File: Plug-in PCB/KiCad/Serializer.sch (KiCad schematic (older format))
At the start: 32 parts, among them J1 Conn_Coaxial, U1 DS90UB933-Q1

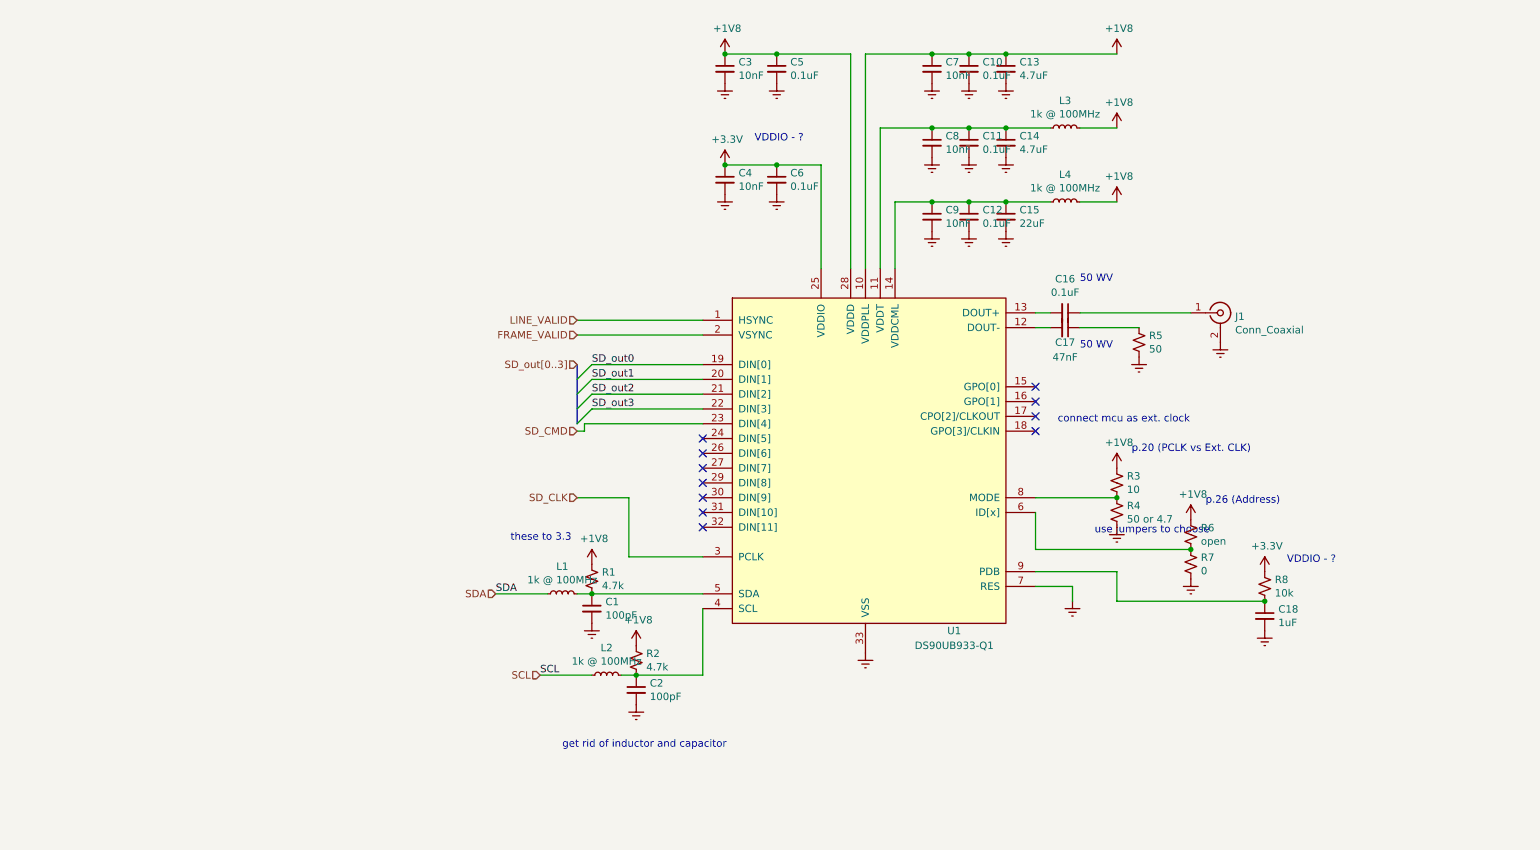
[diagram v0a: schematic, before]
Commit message: Wired Expansion Board Update
1. Begin hardcoding bit-bang communication between wirefree MCU and wired expansion MCU.
++ Can I use the PIO module on the pins to send data in sync while grabbing image from the sensor with parallel capture mode?

2. Wired expansion board schematics and layout modifications
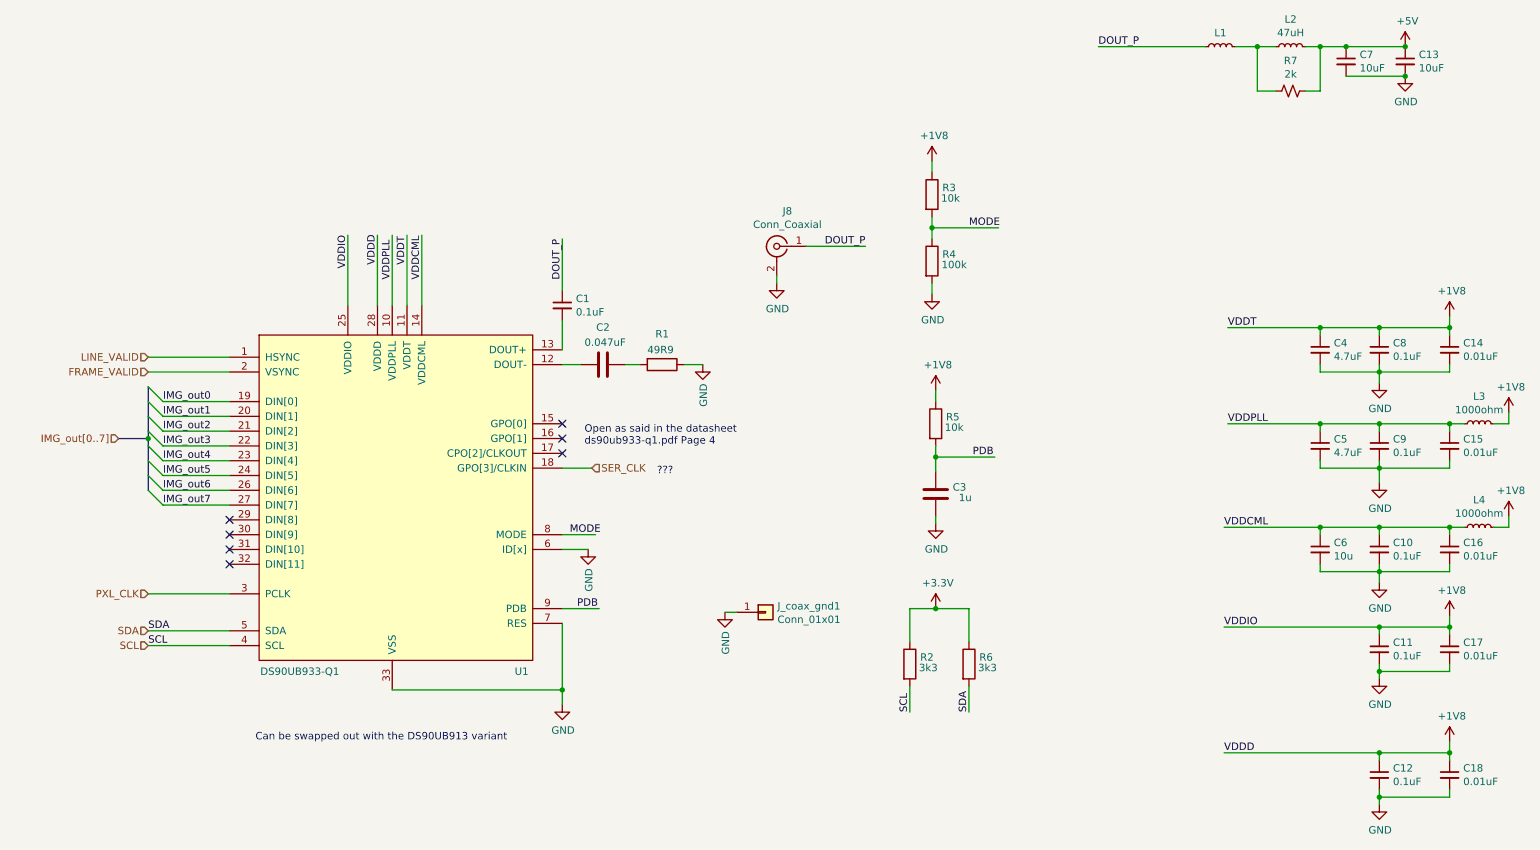
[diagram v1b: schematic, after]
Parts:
- removed C1, C2: GQM1875C2E101JB12D, .Capacitor:C_0603_1608Metric_L, symbol .Capacitor:GQM1875C2E101JB12D
- removed C10, C11, C12, C16, C5, C6: GCJ188R71E104KA12D, .Capacitor:C_0603_1608Metric_L, symbol .Capacitor:GCJ188R71E104KA12D
- removed C13, C14: GRM188R61E475KE11D, .Capacitor:C_0603_1608Metric_L, symbol .Capacitor:GRM188R61E475KE11D
- removed C15: GRM21BR61C226ME44L, .Capacitor:C_0805_2012Metric_L, symbol .Capacitor:GRM21BR61C226ME44L
- removed C17: GRM155R71E473KA88D, .Capacitor:C_0402_1005Metric_L, symbol .Capacitor:GRM155R71E473KA88D
- removed C18: GCM21BR71E105KA56L, .Capacitor:C_0805_2012Metric_L, symbol .Capacitor:GCM21BR71E105KA56L
- removed C3, C4, C7, C8, C9: GRM033R71A103KA01D, .Capacitor:C_0201_0603Metric_L, symbol .Capacitor:GRM033R71A103KA01D
- removed J1: Conn_Coaxial, .Connector:SMA-J-P-H-RA-TH1, symbol Connector:Conn_Coaxial
- removed L2: 1k @ 100MHz, .Inductor:L_0603_1608Metric_L, symbol .Device:L_Small
- removed R1, R2: 4.7k, .Resistor:R_0402_1005Metric_ERJ_L, symbol Device:R_Small_US
- removed R3: 10, .Resistor:R_0402_1005Metric_ERJ_L, symbol .Device:R_Small_US
- removed R4: 50 or 4.7, .Resistor:R_0402_1005Metric_ERJ_L, symbol .Device:R_Small_US
- removed R5: 50, .Resistor:R_0402_1005Metric_ERJ_L, symbol Device:R_Small_US
- removed R6: open, .Resistor:R_0402_1005Metric_ERJ_L, symbol .Device:R_Small_US
- removed R8: 10k, .Resistor:R_0402_1005Metric_ERJ_L, symbol .Device:R_Small_US
- added C1: GRM033R61A104ME15D, .Capacitor:C_0201_0603Metric_L, symbol .Capacitor:GRM033R61A104ME15D
- added C10, C11, C12, C8, C9: GRM033R61A104ME15D, .Capacitor:C_0201_0603Metric_L, symbol .Device:C_Small
- added C13, C7: GRM155R60J106ME15D, .Capacitor:C_0402_1005Metric_L, symbol .Capacitor:GRM155R60J106ME15D
- added C14, C15, C16, C17, C18: GRM033R71A103KA01D, .Capacitor:C_0201_0603Metric_L, symbol .Device:C_Small
- added C2: GRM033R61C473KE84D, .Capacitor:C_0201_0603Metric_L, symbol .Device:C
- added C3: GRM033R61A105ME15D, .Capacitor:C_0201_0603Metric_L, symbol .Device:C
- added C4, C5: GRM155R60J475ME47D, .Capacitor:C_0402_1005Metric_L, symbol .Device:C_Small
- added C6: GRJ155R60J106ME11D, .Capacitor:C_0402_1005Metric_L, symbol .Device:C_Small
- added J8: Conn_Coaxial, .Connector:U_FL-R-SMT_10_, symbol Connector:Conn_Coaxial
- added J_coax_gnd1: Conn_01x01, .Connector:Conn_1x1_100x100_Pad, symbol .Connector:Conn_01x01
- added L2: ADL3225V-470MT-TL000, .Inductor:L_1210_3225Metric_L, symbol .Inductor:ADL3225V-470MT-TL000
- added R1: ERJ-1GEF49R9C, .Resistor:R_0201_0603Metric_ERJ_L, symbol Device:R
- added R2, R6: ERJ-1GEF3321C, .Resistor:R_0201_0603Metric_ERJ_L, symbol Device:R
- added R3, R5: ERJ-1GEF1002C, .Resistor:R_0201_0603Metric_ERJ_L, symbol Device:R
- added R4: ERJ-1GEF1003C, .Resistor:R_0201_0603Metric_ERJ_L, symbol Device:R
- L1, L3, L4: value 1k @ 100MHz -> BLM15HD102SN1D; footprint .Inductor:L_0603_1608Metric_L -> Inductor_SMD:L_0402_1005Metric; Note (none) -> 1000ohm
- R7: value 0 -> MMBT3904LP-7B; footprint .Resistor:R_0402_1005Metric_ERJ_L -> .Resistor:R_0201_0603Metric_ERJ_L; Note (none) -> 2k; Size (none) -> 0201
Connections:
- net labels added: +5V, DOUT_P, GND, IMG_out0, IMG_out1, IMG_out2, IMG_out3, IMG_out4, IMG_out5, IMG_out6, IMG_out7, IMG_out[0..7], MODE, PDB, PXL_CLK, SER_CLK, VDDCML, VDDD, VDDIO, VDDPLL, VDDT
- net labels removed: Earth, SD_CLK, SD_CMD, SD_out0, SD_out1, SD_out2, SD_out3, SD_out[0..3]
- wire segments 54 -> 121
- no-connect marks 11 -> 7
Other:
- note added: "???"
- note added: "Can be swapped out with the DS90UB913 variant"
- note added: "Open as said in the datasheet\nds90ub933-q1.pdf Page 4"
- note removed: "50 WV"
- note removed: "VDDIO - ?"
- note removed: "connect mcu as ext. clock"
- note removed: "get rid of inductor and capacitor"
- note removed: "p.20 (PCLK vs Ext. CLK)"
- note removed: "p.26 (Address)"
- note removed: "these to 3.3"
- note removed: "use jumpers to choose"

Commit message: Wired Expansion Board Updates
1. KiCad: Schematics and layouts completed/Gerber files generated
2. Atmel: Communication protocol from WireFree to WiredExpansion written
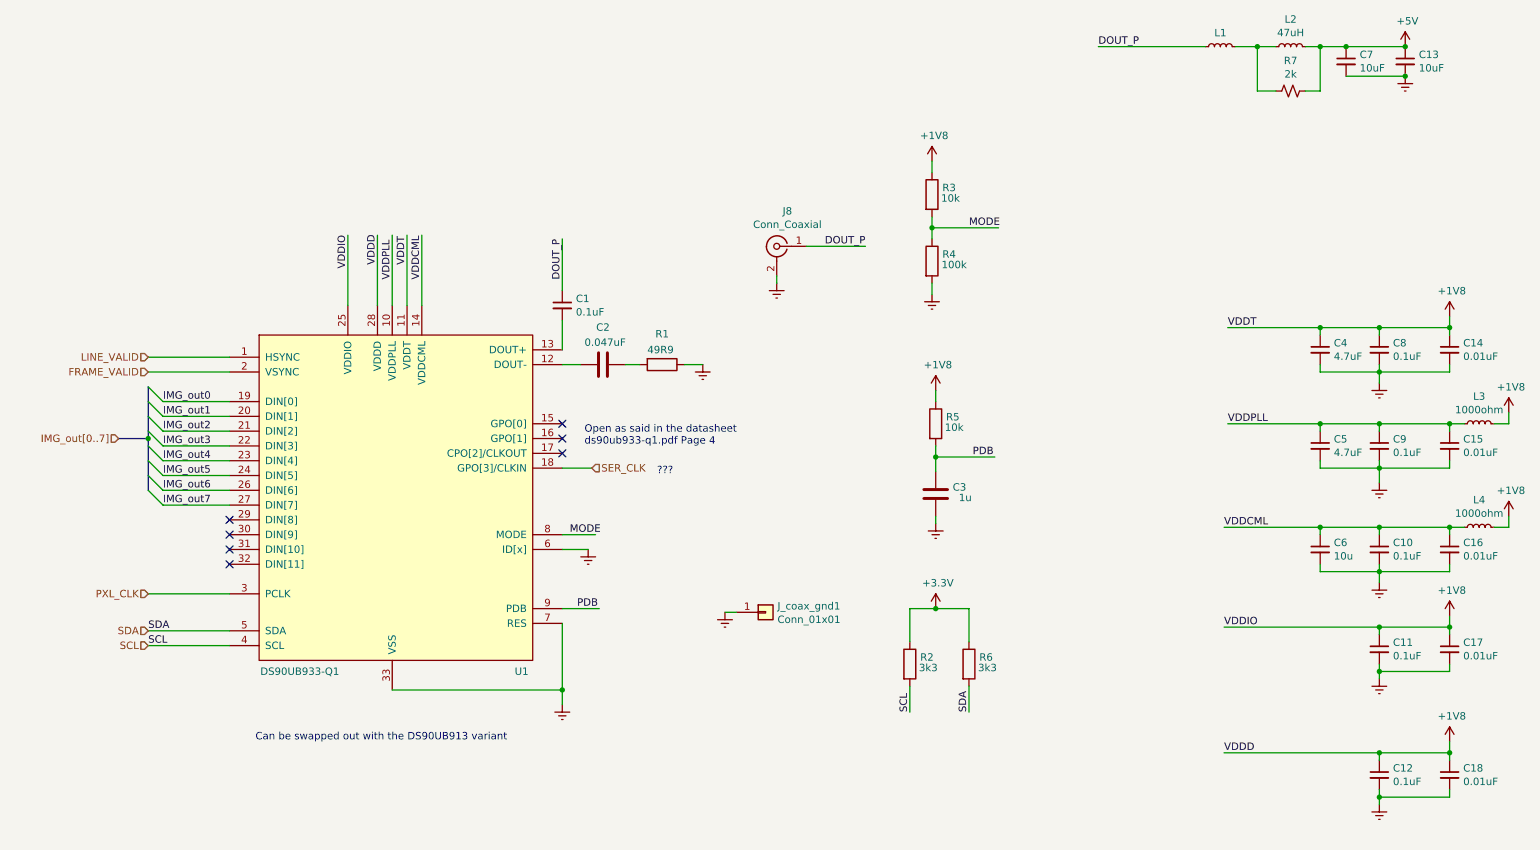
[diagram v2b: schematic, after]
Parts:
- J_coax_gnd1: footprint .Connector:Conn_1x1_100x100_Pad -> .Connector:Conn_1x1_700_Circular_Pad
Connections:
- net labels added: Earth
- net labels removed: GND
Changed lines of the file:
@@
 	9550 1150 9950 1150
-$Comp
-L power:GND #PWR0101
-U 1 1 5C9F5735
-P 9950 1150
-F 0 "#PWR0101" H 9950 900 50  0001 C CNN
-F 1 "GND" H 9955 977 50  0000 C CNN
-F 2 "" H 9950 1150 50  0001 C CNN
-F 3 "" H 9950 1150 50  0001 C CNN
-	1    9950 1150
-	1    0    0    -1
-$EndComp
-Connection ~ 9950 1150
 $Comp
 L power:+5V #PWR0102
@@
 	4250 4850 4250 5300
 $Comp
-L power:GND #PWR0107
-U 1 1 5CC5A56A
-P 4250 5400
-F 0 "#PWR0107" H 4250 5150 50  0001 C CNN
-F 1 "GND" H 4255 5227 50  0000 C CNN
-F 2 "" H 4250 5400 50  0001 C CNN
-F 3 "" H 4250 5400 50  0001 C CNN
-	1    4250 5400
-	1    0    0    -1
-$EndComp
-$Comp
 L .SERDES:DS90UB933-Q1 U1
 U 1 1 5C9C800D
@@
 Wire Wire Line
 	9775 4500 9375 4500
-$Comp
-L power:GND #PWR0108
-U 1 1 5CC8722C
-P 9775 6075
-F 0 "#PWR0108" H 9775 5825 50  0001 C CNN
-F 1 "GND" H 9780 5902 50  0000 C CNN
-F 2 "" H 9775 6075 50  0001 C CNN
-F 3 "" H 9775 6075 50  0001 C CNN
-	1    9775 6075
-	1    0    0    -1
-$EndComp
 Wire Wire Line
 	10250 6025 9775 6025
@@
 	10250 3800 9775 3800
 Connection ~ 9775 3800
-$Comp
-L power:GND #PWR0112
-U 1 1 5CCECEF1
-P 9775 3225
-F 0 "#PWR0112" H 9775 2975 50  0001 C CNN
-F 1 "GND" H 9780 3052 50  0000 C CNN
-F 2 "" H 9775 3225 50  0001 C CNN
-F 3 "" H 9775 3225 50  0001 C CNN
-	1    9775 3225
-	1    0    0    -1
-$EndComp
-$Comp
-L power:GND #PWR0113
-U 1 1 5CCED832
-P 9775 3900
-F 0 "#PWR0113" H 9775 3650 50  0001 C CNN
-F 1 "GND" H 9780 3727 50  0000 C CNN
-F 2 "" H 9775 3900 50  0001 C CNN
-F 3 "" H 9775 3900 50  0001 C CNN
-	1    9775 3900
-	1    0    0    -1
-$EndComp
-$Comp
-L power:GND #PWR0114
-U 1 1 5CCEDC35
-P 9775 4575
-F 0 "#PWR0114" H 9775 4325 50  0001 C CNN
-F 1 "GND" H 9780 4402 50  0000 C CNN
-F 2 "" H 9775 4575 50  0001 C CNN
-F 3 "" H 9775 4575 50  0001 C CNN
-	1    9775 4575
-	1    0    0    -1
-$EndComp
 Wire Wire Line
 	9775 3225 9775 3150
@@
 Wire Wire Line
 	4675 3100 4775 3100
-$Comp
-L power:GND #PWR0115
-U 1 1 5CD1913A
-P 5200 3100
-F 0 "#PWR0115" H 5200 2850 50  0001 C CNN
-F 1 "GND" V 5205 2972 50  0000 R CNN
-F 2 "" H 5200 3100 50  0001 C CNN
-F 3 "" H 5200 3100 50  0001 C CNN
-	1    5200 3100
-	1    0    0    -1
-$EndComp
 Wire Wire Line
 	5075 3100 5200 3100
-$Comp
-L power:GND #PWR0116
-U 1 1 5CD1E39A
-P 4425 4350
-F 0 "#PWR0116" H 4425 4100 50  0001 C CNN
-F 1 "GND" V 4430 4222 50  0000 R CNN
-F 2 "" H 4425 4350 50  0001 C CNN
-F 3 "" H 4425 4350 50  0001 C CNN
-	1    4425 4350
-	1    0    0    -1
-$EndComp
 Wire Wire Line
 	4250 4350 4425 4350
@@
 Text Notes 4400 3650 0    50   ~ 0
 Open as said in the datasheet\nds90ub933-q1.pdf Page 4
-$Comp
-L power:GND #PWR0117
-U 1 1 5CD64A42
-P 9775 5225
-F 0 "#PWR0117" H 9775 4975 50  0001 C CNN
-F 1 "GND" H 9780 5052 50  0000 C CNN
-F 2 "" H 9775 5225 50  0001 C CNN
-F 3 "" H 9775 5225 50  0001 C CNN
-	1    9775 5225
-	1    0    0    -1
-$EndComp
 Wire Wire Line
 	10250 5175 9775 5175
@@
 Wire Wire Line
 	6750 2100 6750 2175
-$Comp
-L power:GND #PWR0120
-U 1 1 5CDE9C95
-P 6750 2625
-F 0 "#PWR0120" H 6750 2375 50  0001 C CNN
-F 1 "GND" H 6755 2452 50  0000 C CNN
-F 2 "" H 6750 2625 50  0001 C CNN
-F 3 "" H 6750 2625 50  0001 C CNN
-	1    6750 2625
-	1    0    0    -1
-$EndComp
 Wire Wire Line
 	6750 2550 6750 2625
@@
 Wire Wire Line
 	6775 3650 6775 3725
-$Comp
-L power:GND #PWR0122
-U 1 1 5CDF8F1D
-P 6775 4175
-F 0 "#PWR0122" H 6775 3925 50  0001 C CNN
-F 1 "GND" H 6780 4002 50  0000 C CNN
-F 2 "" H 6775 4175 50  0001 C CNN
-F 3 "" H 6775 4175 50  0001 C CNN
-	1    6775 4175
-	1    0    0    -1
-$EndComp
 Connection ~ 6775 3725
 $Comp
@@
 	0    1    1    0
 $EndComp
-$Comp
-L power:GND #PWR0130
-U 1 1 5CCC6379
-P 5700 2550
-F 0 "#PWR0130" H 5700 2300 50  0001 C CNN
-F 1 "GND" H 5705 2377 50  0000 C CNN
-F 2 "" H 5700 2550 50  0001 C CNN
-F 3 "" H 5700 2550 50  0001 C CNN
-	1    5700 2550
-	1    0    0    -1
-$EndComp
 Wire Wire Line
 	5700 2500 5700 2550
@@
 F 0 "J_coax_gnd1" H 5705 4817 50  0000 L CNN
 F 1 "Conn_01x01" H 5705 4726 50  0000 L CNN
-F 2 ".Connector:Conn_1x1_100x100_Pad" H 5625 4775 50  0001 C CNN
+F 2 ".Connector:Conn_1x1_700_Circular_Pad" H 5625 4775 50  0001 C CNN
 F 3 "~" H 5625 4775 50  0001 C CNN
 	1    5625 4775
-	1    0    0    -1
-$EndComp
-$Comp
-L power:GND #PWR0131
-U 1 1 5CD112FF
-P 5350 4775
-F 0 "#PWR0131" H 5350 4525 50  0001 C CNN
-F 1 "GND" V 5355 4647 50  0000 R CNN
-F 2 "" H 5350 4775 50  0001 C CNN
-F 3 "" H 5350 4775 50  0001 C CNN
-	1    5350 4775
 	1    0    0    -1
 $EndComp
@@
 Wire Wire Line
 	8725 5725 9775 5725
+Text Label 8725 5725 0    50   ~ 0
+VDDD
+$Comp
+L power:Earth #PWR0101
+U 1 1 5D5F42F2
+P 4250 5400
+F 0 "#PWR0101" H 4250 5150 50  0001 C CNN
+F 1 "Earth" H 4250 5250 50  0001 C CNN
+F 2 "" H 4250 5400 50  0001 C CNN
+F 3 "~" H 4250 5400 50  0001 C CNN
+	1    4250 5400
+	1    0    0    -1
+$EndComp
+$Comp
+L power:Earth #PWR0103
+U 1 1 5D5F47B7
+P 4425 4350
+F 0 "#PWR0103" H 4425 4100 50  0001 C CNN
+F 1 "Earth" H 4425 4200 50  0001 C CNN
+F 2 "" H 4425 4350 50  0001 C CNN
+F 3 "~" H 4425 4350 50  0001 C CNN
+	1    4425 4350
+	1    0    0    -1
+$EndComp
+$Comp
+L power:Earth #PWR0104
+U 1 1 5D5F4C82
+P 5350 4775
+F 0 "#PWR0104" H 5350 4525 50  0001 C CNN
+F 1 "Earth" H 5350 4625 50  0001 C CNN
+F 2 "" H 5350 4775 50  0001 C CNN
+F 3 "~" H 5350 4775 50  0001 C CNN
+	1    5350 4775
+	1    0    0    -1
+$EndComp
+$Comp
+L power:Earth #PWR0105
+U 1 1 5D5F5153
+P 5200 3100
+F 0 "#PWR0105" H 5200 2850 50  0001 C CNN
+F 1 "Earth" H 5200 2950 50  0001 C CNN
+F 2 "" H 5200 3100 50  0001 C CNN
+F 3 "~" H 5200 3100 50  0001 C CNN
+	1    5200 3100
+	1    0    0    -1
+$EndComp
+$Comp
+L power:Earth #PWR0106
+U 1 1 5D5F562A
+P 5700 2550
+F 0 "#PWR0106" H 5700 2300 50  0001 C CNN
+F 1 "Earth" H 5700 2400 50  0001 C CNN
+F 2 "" H 5700 2550 50  0001 C CNN
+F 3 "~" H 5700 2550 50  0001 C CNN
+	1    5700 2550
+	1    0    0    -1
+$EndComp
+$Comp
+L power:Earth #PWR0107
+U 1 1 5D5F5B07
+P 6750 2625
+F 0 "#PWR0107" H 6750 2375 50  0001 C CNN
+F 1 "Earth" H 6750 2475 50  0001 C CNN
+F 2 "" H 6750 2625 50  0001 C CNN
+F 3 "~" H 6750 2625 50  0001 C CNN
+	1    6750 2625
+	1    0    0    -1
+$EndComp
+$Comp
+L power:Earth #PWR0108
+U 1 1 5D5F5FEA
+P 6775 4175
+F 0 "#PWR0108" H 6775 3925 50  0001 C CNN
+F 1 "Earth" H 6775 4025 50  0001 C CNN
+F 2 "" H 6775 4175 50  0001 C CNN
+F 3 "~" H 6775 4175 50  0001 C CNN
+	1    6775 4175
+	1    0    0    -1
+$EndComp
+$Comp
+L power:Earth #PWR0112
+U 1 1 5D5F64D3
+P 9950 1150
+F 0 "#PWR0112" H 9950 900 50  0001 C CNN
+F 1 "Earth" H 9950 1000 50  0001 C CNN
+F 2 "" H 9950 1150 50  0001 C CNN
+F 3 "~" H 9950 1150 50  0001 C CNN
+	1    9950 1150
+	1    0    0    -1
+$EndComp
+Connection ~ 9950 1150
+$Comp
+L power:Earth #PWR0113
+U 1 1 5D5F69C2
+P 9775 3225
+F 0 "#PWR0113" H 9775 2975 50  0001 C CNN
+F 1 "Earth" H 9775 3075 50  0001 C CNN
+F 2 "" H 9775 3225 50  0001 C CNN
+F 3 "~" H 9775 3225 50  0001 C CNN
+	1    9775 3225
+	1    0    0    -1
+$EndComp
+$Comp
+L power:Earth #PWR0114
+U 1 1 5D5F6EB7
+P 9775 3900
+F 0 "#PWR0114" H 9775 3650 50  0001 C CNN
+F 1 "Earth" H 9775 3750 50  0001 C CNN
+F 2 "" H 9775 3900 50  0001 C CNN
+F 3 "~" H 9775 3900 50  0001 C CNN
+	1    9775 3900
+	1    0    0    -1
+$EndComp
+$Comp
+L power:Earth #PWR0115
+U 1 1 5D5F73A0
+P 9775 4575
+F 0 "#PWR0115" H 9775 4325 50  0001 C CNN
+F 1 "Earth" H 9775 4425 50  0001 C CNN
+F 2 "" H 9775 4575 50  0001 C CNN
+F 3 "~" H 9775 4575 50  0001 C CNN
+	1    9775 4575
+	1    0    0    -1
+$EndComp
+$Comp
+L power:Earth #PWR0116
+U 1 1 5D5F788F
+P 9775 5225
+F 0 "#PWR0116" H 9775 4975 50  0001 C CNN
+F 1 "Earth" H 9775 5075 50  0001 C CNN
+F 2 "" H 9775 5225 50  0001 C CNN
+F 3 "~" H 9775 5225 50  0001 C CNN
+	1    9775 5225
+	1    0    0    -1
+$EndComp
+$Comp
+L power:Earth #PWR0117
+U 1 1 5D5F7D84
+P 9775 6075
+F 0 "#PWR0117" H 9775 5825 50  0001 C CNN
+F 1 "Earth" H 9775 5925 50  0001 C CNN
+F 2 "" H 9775 6075 50  0001 C CNN
+F 3 "~" H 9775 6075 50  0001 C CNN
+	1    9775 6075
+	1    0    0    -1
+$EndComp
 Wire Bus Line
 	1450 3250 1450 3600
 Wire Bus Line
 	1450 3600 1450 3950
-Text Label 8725 5725 0    50   ~ 0
-VDDD
 $EndSCHEMATC
